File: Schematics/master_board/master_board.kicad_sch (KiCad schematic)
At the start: 52 parts, among them J1 2x5x1.27mm, J2 USB_C_Receptacle_USB2.0, J3 Conn_01x01_Female, J4 Conn_01x01_Female, J5 Conn_01x01_Female, J6 Conn_01x01_Female, SW1 SW_Push, SW2 SW_Push, SW3 SW_Push, U1 NCP1117-3.3_SOT223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

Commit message: bom generation script
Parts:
- C1, C2: Manufacturer (none) -> Samsung Electro-Mechanics; Manufacturer Part Number (none) -> CL21A106KOQNNNG
- C10, C11, C14, C15, C16, C17, C3, C4, C5, C8, C9: Manufacturer (none) -> Venkel; Manufacturer Part Number (none) -> C0402X7R100-104KNE-CT
- C12, C13: Manufacturer (none) -> Venkel; Manufacturer Part Number (none) -> C0402C0G250-270JNE-CT
- C6, C7: Manufacturer (none) -> Venkel; Manufacturer Part Number (none) -> C0402X5R6R3-105KNP-CT
- D1: Manufacturer (none) -> CreeLED, Inc.; Manufacturer Part Number (none) -> UHD111A-FKA-C3K23E1L3VG5ZB3Z3
- J1: Manufacturer (none) -> CNC Tech; Manufacturer Part Number (none) -> CONN HEADER SMD 10POS 1.27MM
- J2: Manufacturer (none) -> GCT; Manufacturer Part Number (none) -> USB4105-GF-A
- R1, R14, R16, R17, R2, R3: Manufacturer (none) -> YAGEO; Manufacturer Part Number (none) -> RC0402FR-7W1KL
- R10, R11: Manufacturer (none) -> TE Connectivity Passive Product; Manufacturer Part Number (none) -> CRGP0402F27R
- R12, R13, R15, R9: Manufacturer (none) -> YAGEO; Manufacturer Part Number (none) -> RC0402JR-7W10KL
- R4, R5, R6: Manufacturer (none) -> YAGEO; Manufacturer Part Number (none) -> RC0402FR-7W49R9L
- R7, R8: Manufacturer (none) -> Panasonic Electronic Components; Manufacturer Part Number (none) -> ERJ-2RKF5101X
- SW1, SW2, SW3: Manufacturer (none) -> C&K; Manufacturer Part Number (none) -> D6C40 F1 LFS
- U1: Manufacturer (none) -> onsemi; Manufacturer Part Number (none) -> NCP1117LPST33T3G
- U2: Manufacturer (none) -> Raspberry Pi; Manufacturer Part Number (none) -> SC0914(13)
- U3: Manufacturer (none) -> Winbond Electronics; Manufacturer Part Number (none) -> W25Q16JVSSIQ
- Y1: Manufacturer (none) -> Abracon LLC; Manufacturer Part Number (none) -> ABLS-12.000MHZ-B4-T

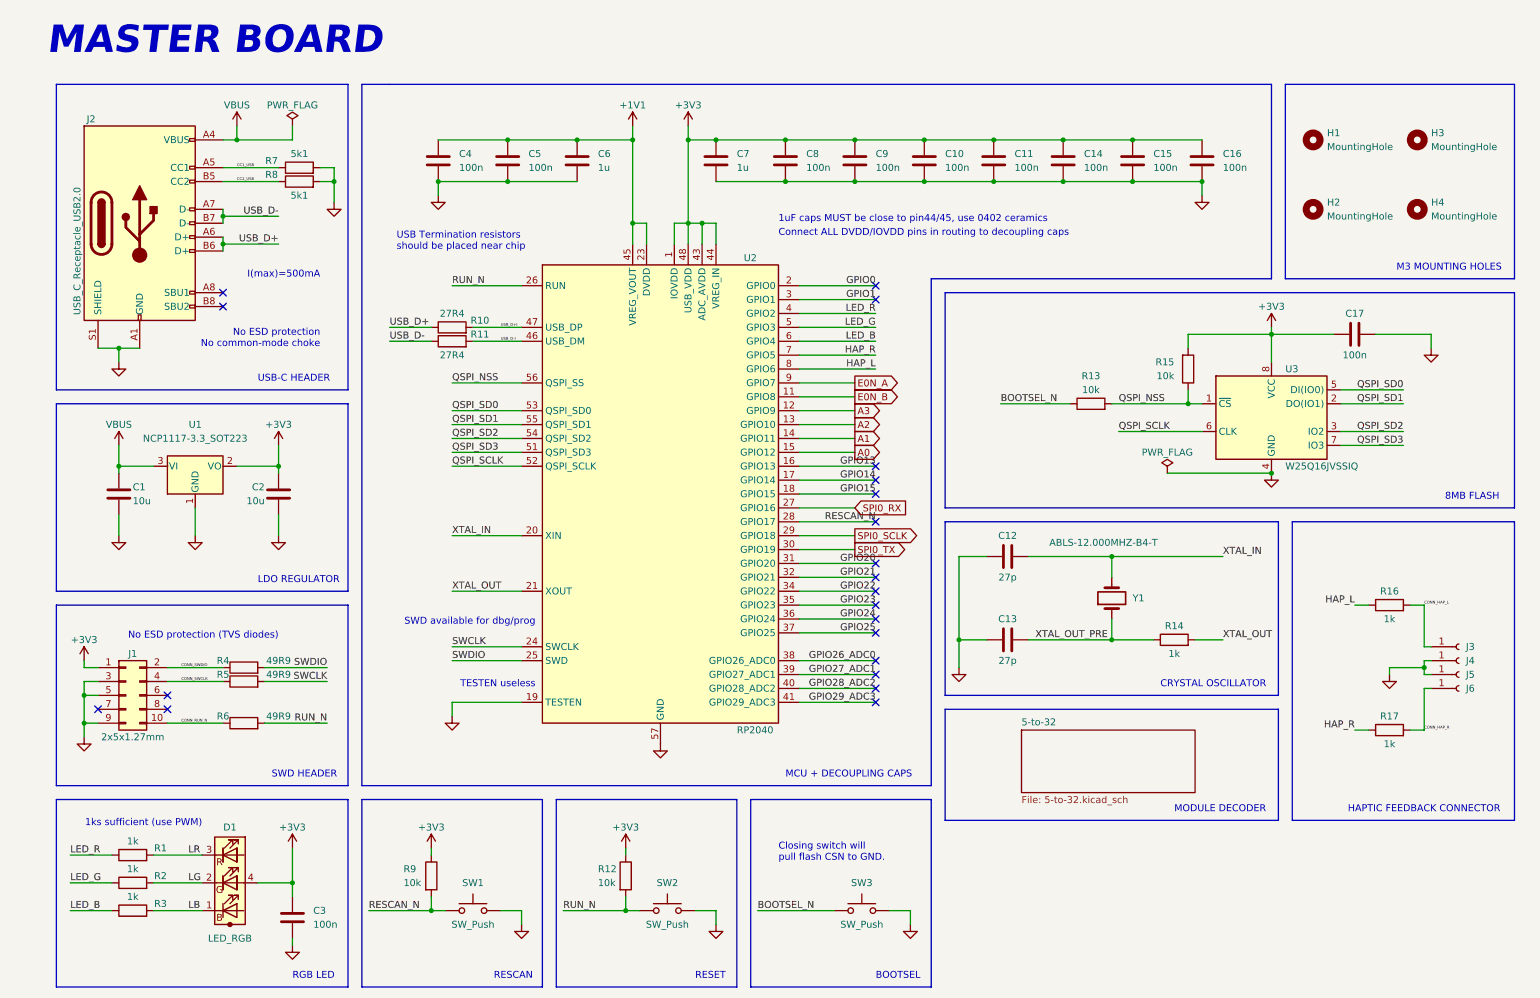
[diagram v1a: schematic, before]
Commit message: Changed 10k res values to 1k, SWD pins, Decoder footprints, and haptic pins
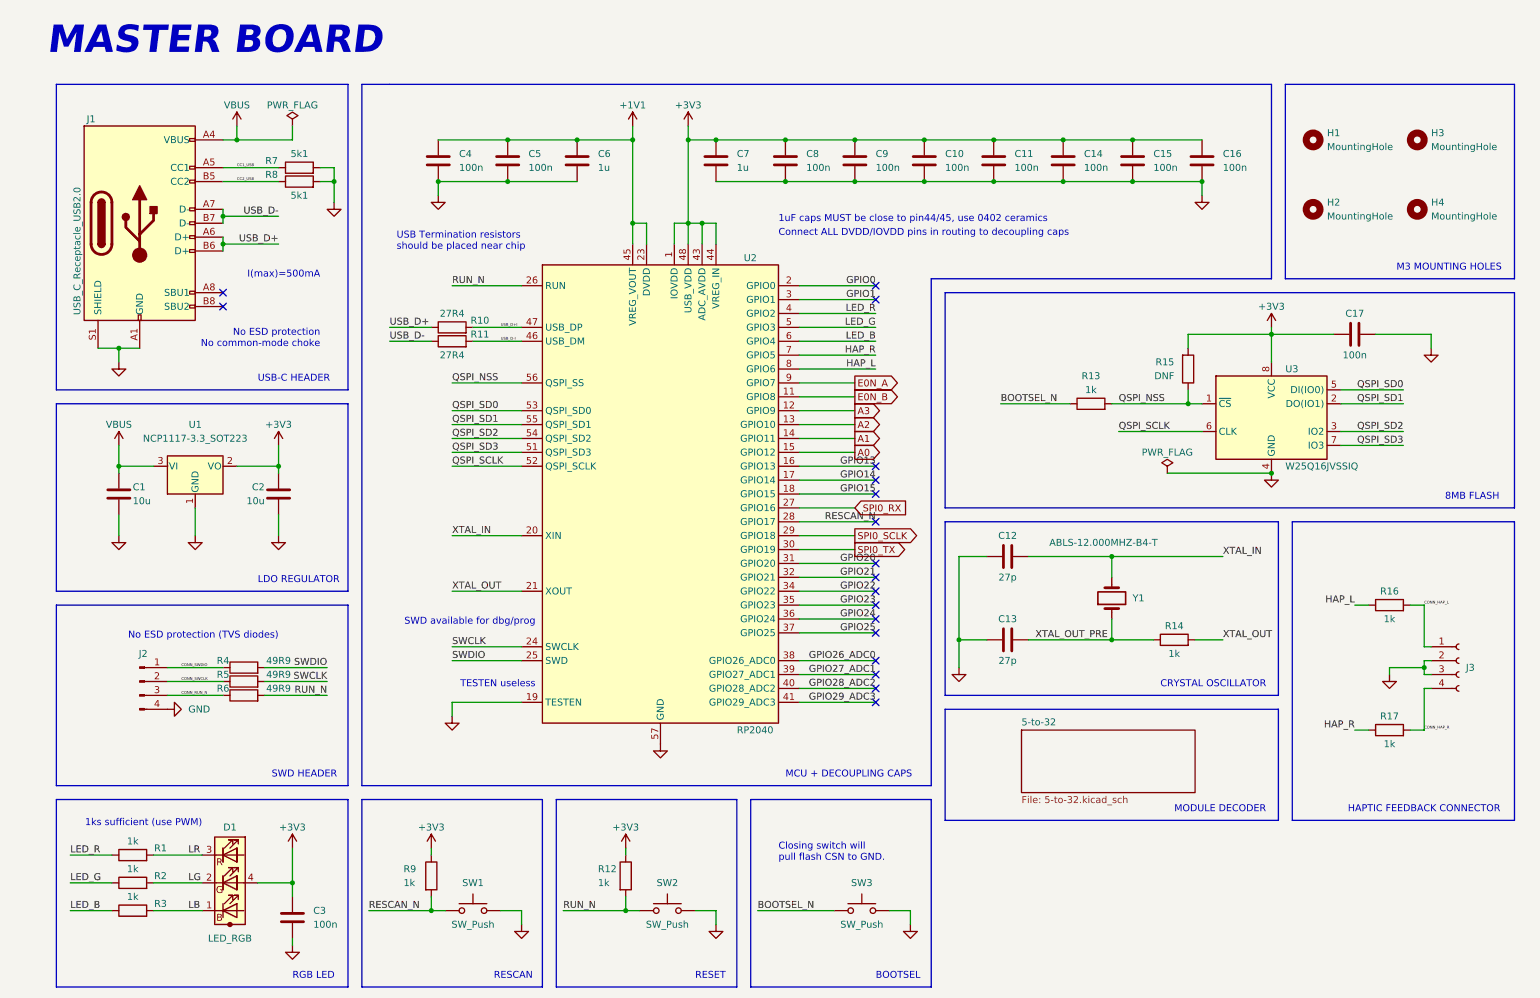
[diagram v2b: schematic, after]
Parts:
- removed J1: 2x5x1.27mm, Connector_PinHeader_1.27mm:PinHeader_2x05_P1.27mm_Vertical_SMD, symbol Connector_Generic:Conn_02x05_Odd_Even
- removed J3, J4, J5, J6: Conn_01x01_Female, Connector_PinHeader_2.54mm:PinHeader_1x01_P2.54mm_Vertical, symbol Connector:Conn_01x01_Female
- added J2: Conn_01x04_Male, Connector_PinHeader_2.54mm:PinHeader_1x04_P2.54mm_Vertical, symbol Connector:Conn_01x04_Male
- added J3: Conn_01x04_Female, Connector_PinHeader_2.54mm:PinHeader_1x04_P2.54mm_Vertical, symbol Connector:Conn_01x04_Female
- R12, R13, R9: value 10k -> 1k
- R15: value 10k -> DNF
- renumbered J2 to J1
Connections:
- net CONN_HAP_L: now also J3.1 (Pin_1)
- net CONN_HAP_R: now also J3.4 (Pin_4)
- net CONN_RUN_N: now also J2.3 (Pin_3)
- net CONN_SWCLK: now also J2.2 (Pin_2)
- net CONN_SWDIO: now also J2.1 (Pin_1)
- net GND: now also J2.4 (Pin_4), J3.2 (Pin_2), J3.3 (Pin_3)
- no-connect marks 21 -> 18
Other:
- moved on the sheet: R6
